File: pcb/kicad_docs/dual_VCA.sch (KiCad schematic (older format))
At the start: 22 parts, among them J1 signal_in_1, J2 CV_in_1, J3 signal_in_2, J4 CV_in_2, J5 signal_out_1, J6 signal_out_2, J8 Conn_01x06, J9 Conn_01x06

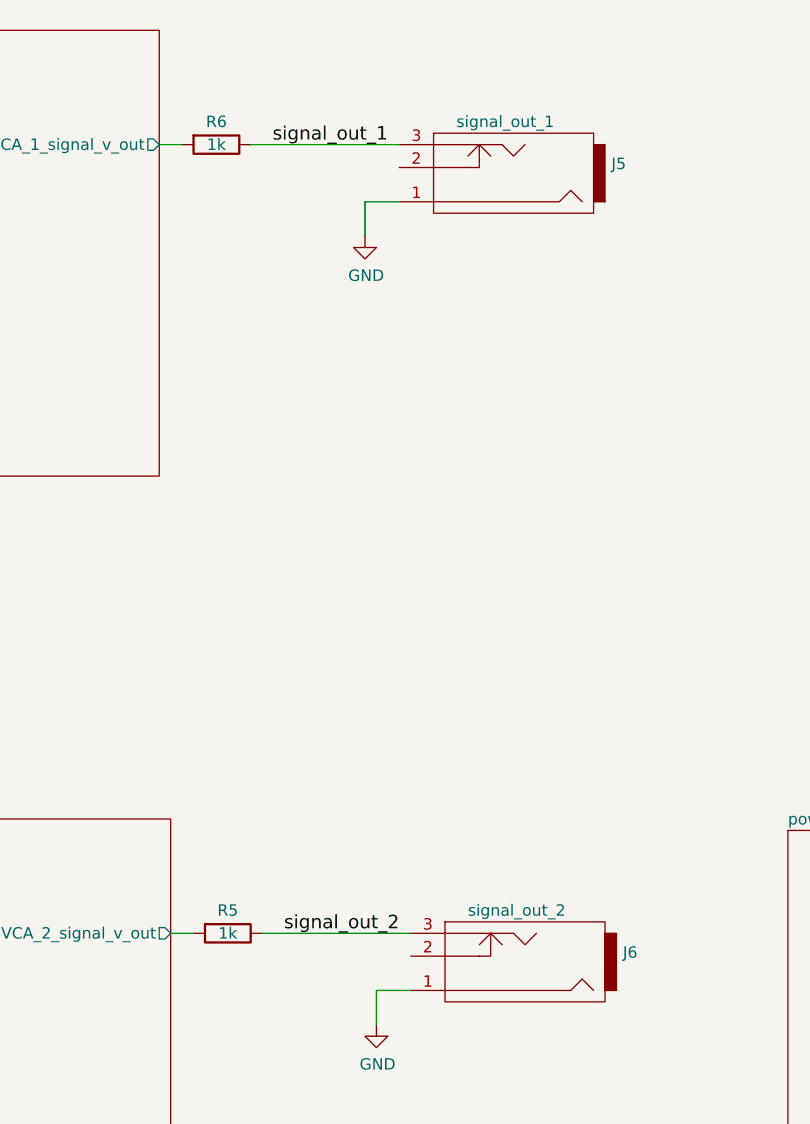
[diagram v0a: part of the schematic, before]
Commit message: add panel, generate interactive BOM
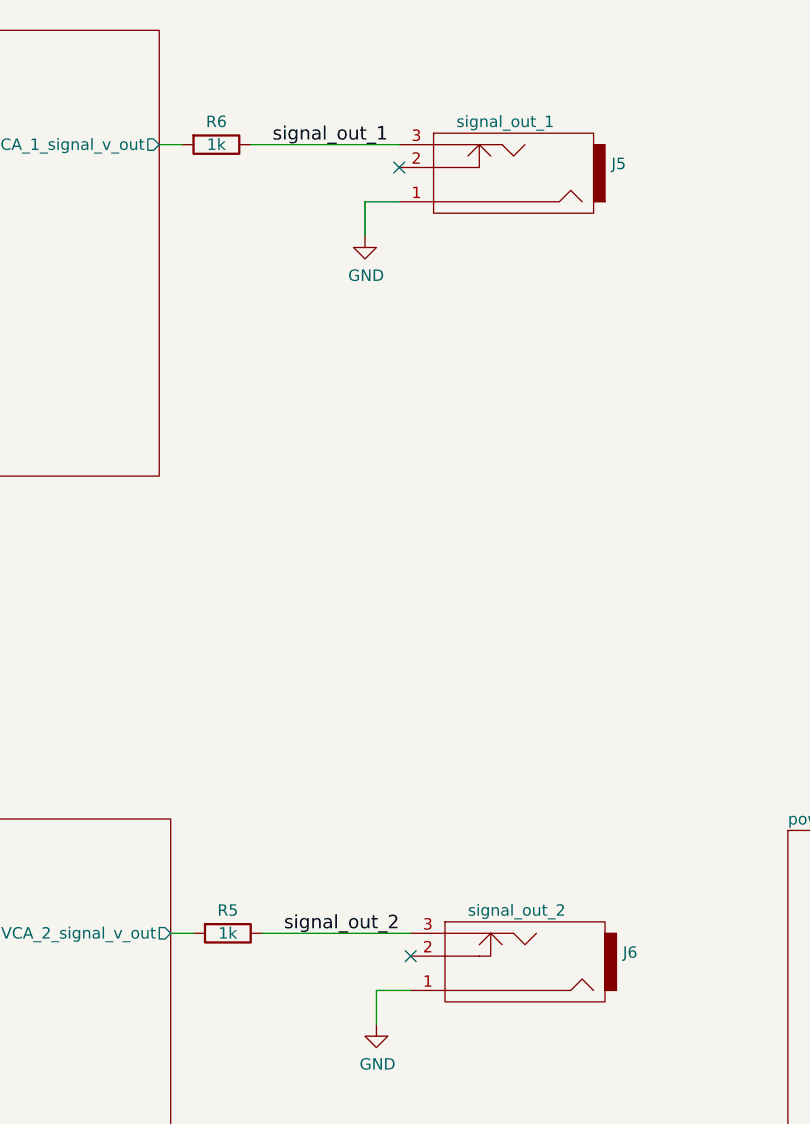
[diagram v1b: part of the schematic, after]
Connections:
- no-connect marks 0 -> 2
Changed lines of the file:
@@
 Text Notes 8650 1350 0    157  ~ 0
 Use these ports \nif wiring by hand,\notherwise do not use
+NoConn ~ 6800 1300
+NoConn ~ 6850 4750
 $EndSCHEMATC
